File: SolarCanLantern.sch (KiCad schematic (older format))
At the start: 16 parts, among them Q1 2N7002, Q2 2N7002, Q3 2N7002, Q4 2N7002, U1 ATTINY13-20SSU

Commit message: add footprints
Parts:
- BT1, SC1: footprint (none) -> Socket_Strips:Socket_Strip_Straight_1x02_Pitch2.54mm
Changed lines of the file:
@@
 $EndComp
 $Comp
-L GND #PWR15
+L GND #PWR01
 U 1 1 5AC18C1B
 P 8200 3750
-F 0 "#PWR15" H 8200 3500 50  0001 C CNN
+F 0 "#PWR01" H 8200 3500 50  0001 C CNN
 F 1 "GND" H 8200 3600 50  0000 C CNN
 F 2 "" H 8200 3750 50  0001 C CNN
@@
 $EndComp
 $Comp
-L +BATT #PWR14
+L +BATT #PWR02
 U 1 1 5AC18C33
 P 8200 3100
-F 0 "#PWR14" H 8200 2950 50  0001 C CNN
+F 0 "#PWR02" H 8200 2950 50  0001 C CNN
 F 1 "+BATT" H 8200 3240 50  0000 C CNN
 F 2 "" H 8200 3100 50  0001 C CNN
@@
 	3250 2950 3250 3150
 $Comp
-L GND #PWR6
+L GND #PWR03
 U 1 1 5AC3EB93
 P 3250 3550
-F 0 "#PWR6" H 3250 3300 50  0001 C CNN
+F 0 "#PWR03" H 3250 3300 50  0001 C CNN
 F 1 "GND" H 3250 3400 50  0000 C CNN
 F 2 "" H 3250 3550 50  0001 C CNN
@@
 $EndComp
 $Comp
-L GND #PWR4
+L GND #PWR04
 U 1 1 5AC3EBB4
 P 2150 3550
-F 0 "#PWR4" H 2150 3300 50  0001 C CNN
+F 0 "#PWR04" H 2150 3300 50  0001 C CNN
 F 1 "GND" H 2150 3400 50  0000 C CNN
 F 2 "" H 2150 3550 50  0001 C CNN
@@
 $EndComp
 $Comp
-L +BATT #PWR3
+L +BATT #PWR05
 U 1 1 5AC3EBCE
 P 2150 2250
-F 0 "#PWR3" H 2150 2100 50  0001 C CNN
+F 0 "#PWR05" H 2150 2100 50  0001 C CNN
 F 1 "+BATT" H 2150 2390 50  0000 C CNN
 F 2 "" H 2150 2250 50  0001 C CNN
@@
 $EndComp
 $Comp
-L +BATT #PWR5
+L +BATT #PWR06
 U 1 1 5AC3EBE8
 P 3250 2250
-F 0 "#PWR5" H 3250 2100 50  0001 C CNN
+F 0 "#PWR06" H 3250 2100 50  0001 C CNN
 F 1 "+BATT" H 3250 2390 50  0000 C CNN
 F 2 "" H 3250 2250 50  0001 C CNN
@@
 	4450 2950 4450 3150
 $Comp
-L GND #PWR8
+L GND #PWR07
 U 1 1 5AC3EE60
 P 4450 3550
-F 0 "#PWR8" H 4450 3300 50  0001 C CNN
+F 0 "#PWR07" H 4450 3300 50  0001 C CNN
 F 1 "GND" H 4450 3400 50  0000 C CNN
 F 2 "" H 4450 3550 50  0001 C CNN
@@
 $EndComp
 $Comp
-L +BATT #PWR7
+L +BATT #PWR08
 U 1 1 5AC3EE66
 P 4450 2250
-F 0 "#PWR7" H 4450 2100 50  0001 C CNN
+F 0 "#PWR08" H 4450 2100 50  0001 C CNN
 F 1 "+BATT" H 4450 2390 50  0000 C CNN
 F 2 "" H 4450 2250 50  0001 C CNN
@@
 	5800 3550 5800 3750
 $Comp
-L GND #PWR9
+L GND #PWR09
 U 1 1 5AC3EF40
 P 5800 4050
-F 0 "#PWR9" H 5800 3800 50  0001 C CNN
+F 0 "#PWR09" H 5800 3800 50  0001 C CNN
 F 1 "GND" H 5800 3900 50  0000 C CNN
 F 2 "" H 5800 4050 50  0001 C CNN
@@
 Switch
 $Comp
-L +BATT #PWR1
+L +BATT #PWR010
 U 1 1 5AC3F242
 P 2100 4600
-F 0 "#PWR1" H 2100 4450 50  0001 C CNN
+F 0 "#PWR010" H 2100 4450 50  0001 C CNN
 F 1 "+BATT" H 2100 4740 50  0000 C CNN
 F 2 "" H 2100 4600 50  0001 C CNN
@@
 $EndComp
 $Comp
-L GND #PWR2
+L GND #PWR011
 U 1 1 5AC3F286
 P 2100 5400
-F 0 "#PWR2" H 2100 5150 50  0001 C CNN
+F 0 "#PWR011" H 2100 5150 50  0001 C CNN
 F 1 "GND" H 2100 5250 50  0000 C CNN
 F 2 "" H 2100 5400 50  0001 C CNN
@@
 F 0 "SC1" H 6800 1700 50  0000 L CNN
 F 1 "Solar_Cell" H 6800 1600 50  0000 L CNN
-F 2 "" V 6700 1660 50  0001 C CNN
+F 2 "Socket_Strips:Socket_Strip_Straight_1x02_Pitch2.54mm" V 6700 1660 50  0001 C CNN
 F 3 "" V 6700 1660 50  0001 C CNN
 	1    6700 1600
@@
 $EndComp
 $Comp
-L GND #PWR12
+L GND #PWR012
 U 1 1 5AC3F62A
 P 6400 2000
-F 0 "#PWR12" H 6400 1750 50  0001 C CNN
+F 0 "#PWR012" H 6400 1750 50  0001 C CNN
 F 1 "GND" H 6400 1850 50  0000 C CNN
 F 2 "" H 6400 2000 50  0001 C CNN
@@
 $EndComp
 $Comp
-L +BATT #PWR13
+L +BATT #PWR013
 U 1 1 5AC3F9A9
 P 7200 1250
-F 0 "#PWR13" H 7200 1100 50  0001 C CNN
+F 0 "#PWR013" H 7200 1100 50  0001 C CNN
 F 1 "+BATT" H 7200 1390 50  0000 C CNN
 F 2 "" H 7200 1250 50  0001 C CNN
@@
 F 0 "BT1" H 6000 5250 50  0000 L CNN
 F 1 "Battery_Cell" H 6000 5150 50  0000 L CNN
-F 2 "" V 5900 5210 50  0001 C CNN
+F 2 "Socket_Strips:Socket_Strip_Straight_1x02_Pitch2.54mm" V 5900 5210 50  0001 C CNN
 F 3 "" V 5900 5210 50  0001 C CNN
 	1    5900 5150
@@
 $EndComp
 $Comp
-L GND #PWR11
+L GND #PWR014
 U 1 1 5AC3FE84
 P 5900 5250
-F 0 "#PWR11" H 5900 5000 50  0001 C CNN
+F 0 "#PWR014" H 5900 5000 50  0001 C CNN
 F 1 "GND" H 5900 5100 50  0000 C CNN
 F 2 "" H 5900 5250 50  0001 C CNN
@@
 $EndComp
 $Comp
-L +BATT #PWR10
+L +BATT #PWR015
 U 1 1 5AC3FEBF
 P 5900 4950
-F 0 "#PWR10" H 5900 4800 50  0001 C CNN
+F 0 "#PWR015" H 5900 4800 50  0001 C CNN
 F 1 "+BATT" H 5900 5090 50  0000 C CNN
 F 2 "" H 5900 4950 50  0001 C CNN

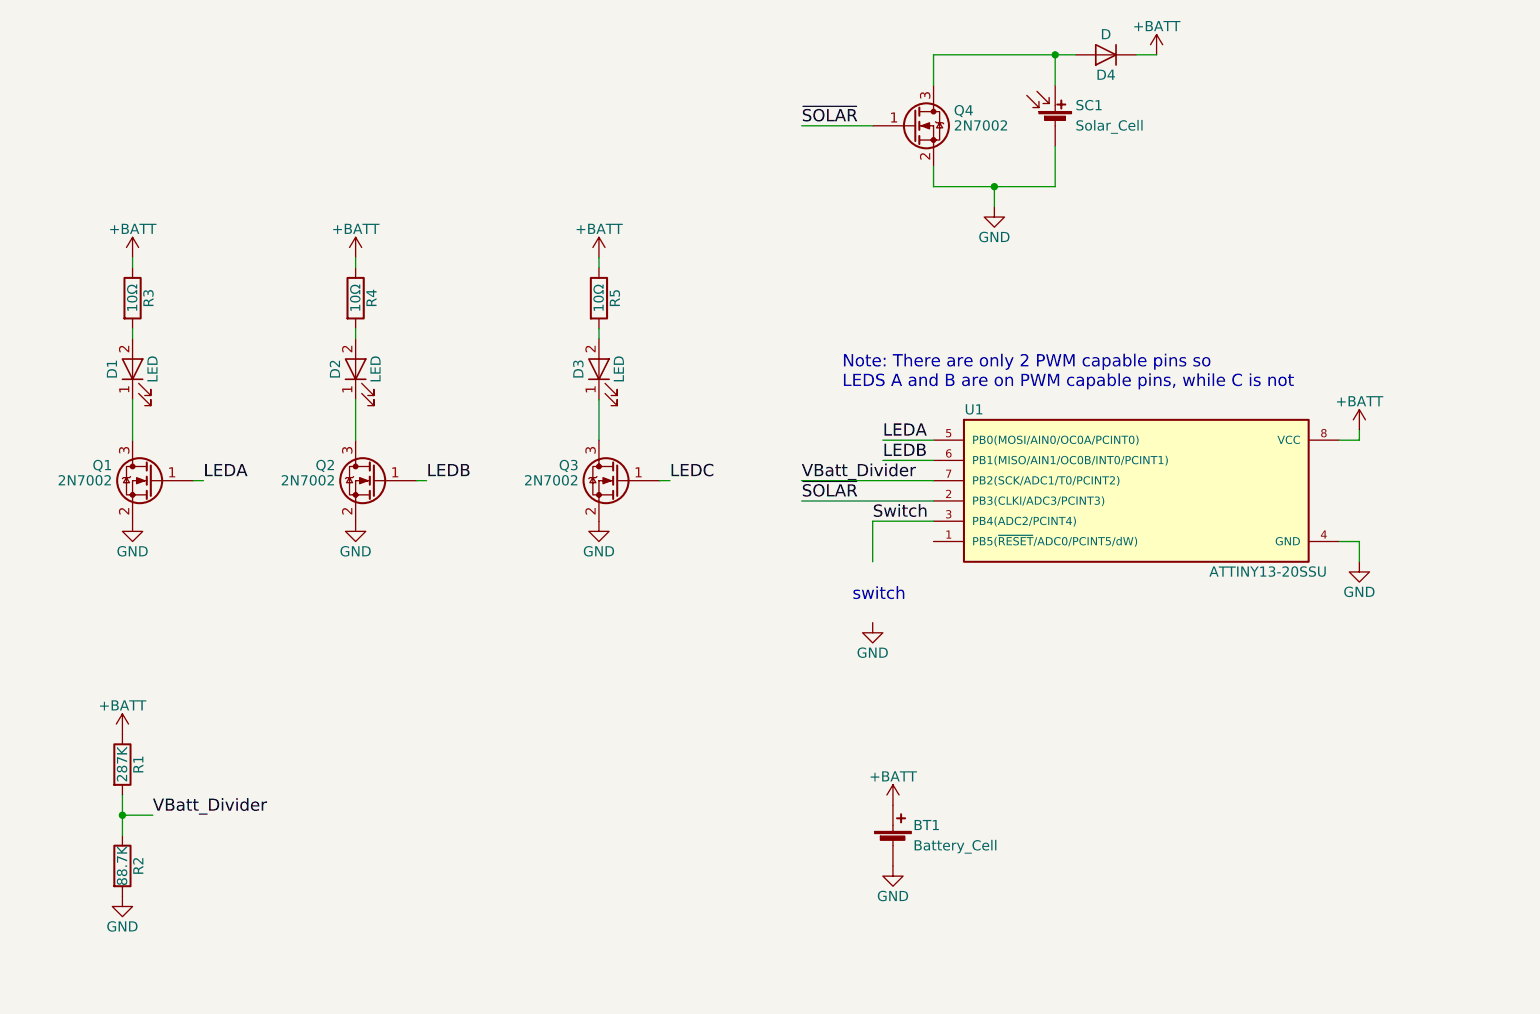
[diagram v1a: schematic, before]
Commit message: first rev pcb layout with no button
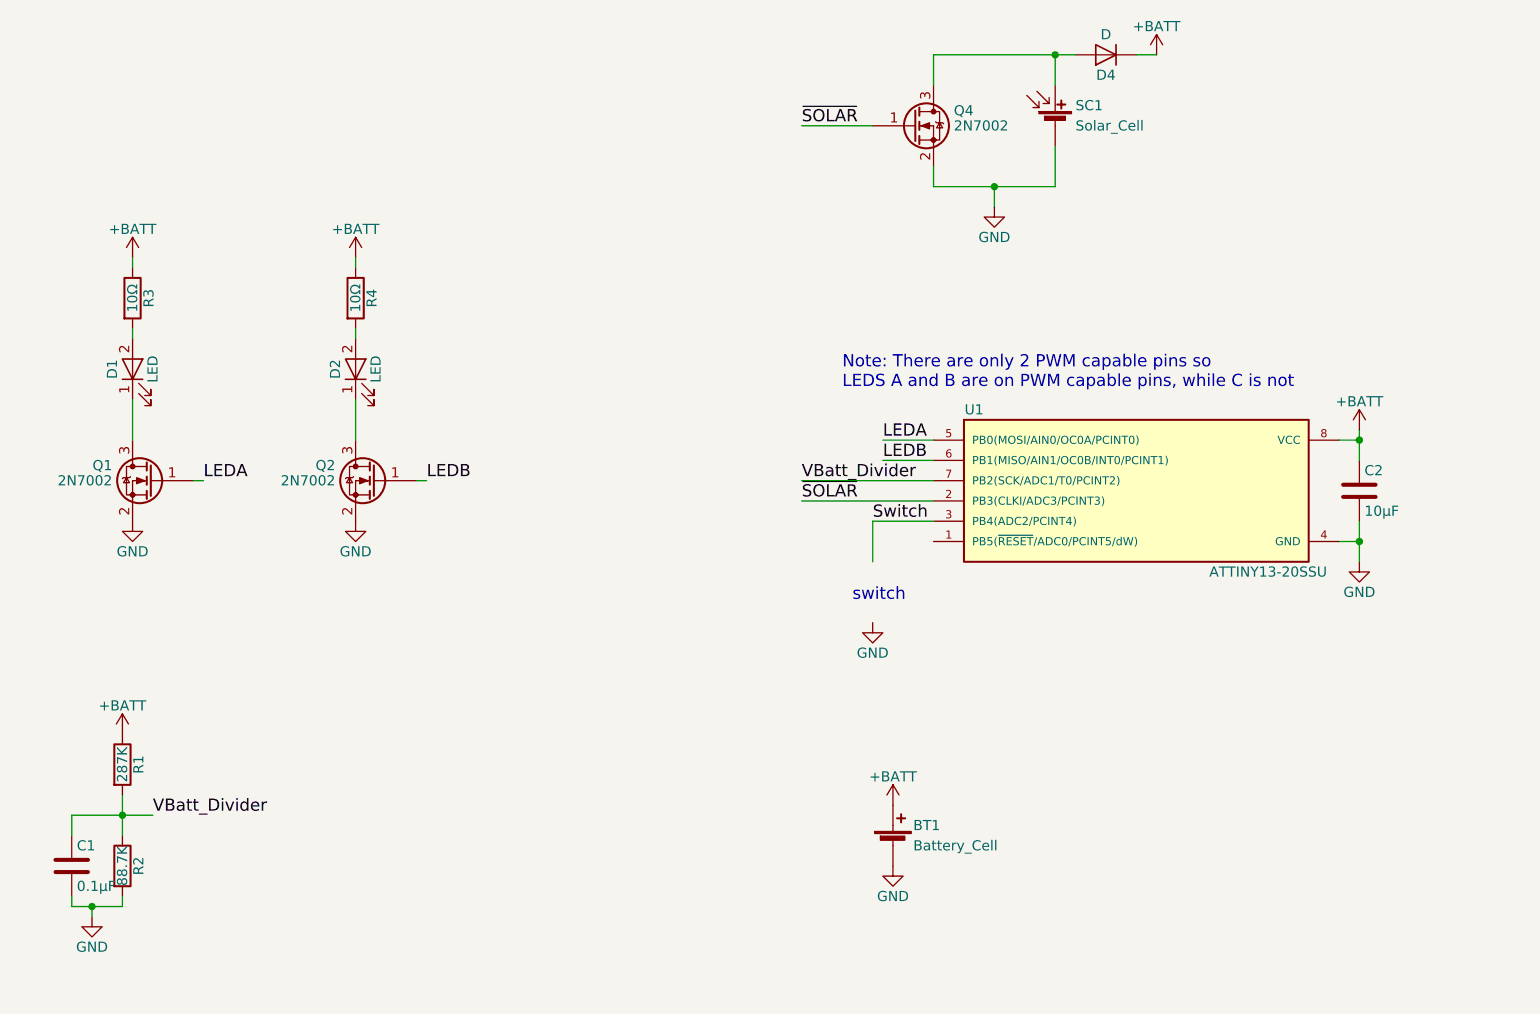
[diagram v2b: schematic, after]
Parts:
- removed D3: LED, LEDs:LED_0805_HandSoldering, symbol LED
- removed Q3: 2N7002, TO_SOT_Packages_SMD:SOT-23, symbol 2N7002
- removed R5: 10Ω, Resistors_SMD:R_0805_HandSoldering, symbol R
- added C1: 0.1µF, Capacitors_SMD:C_0805_HandSoldering, symbol C
- added C2: 10µF, Capacitors_SMD:C_0805_HandSoldering, symbol C
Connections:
- net +BATT: now also C2.1
- net GND: now also C1.2, C2.2
- net VBatt_Divider: now also C1.1
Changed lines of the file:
@@
 LIBS:contrib
 LIBS:valves
+LIBS:battery_management
+LIBS:74xgxx
+LIBS:Altera
+LIBS:analog_devices
+LIBS:dc-dc
+LIBS:stm32
 LIBS:SolarCanLantern-cache
 EELAYER 25 0
@@
 $EndComp
 Wire Wire Line
-	8200 3100 8200 3150
+	8200 3100 8200 3250
 Wire Wire Line
 	8200 3150 8100 3150
@@
 	8100 3650 8200 3650
 Wire Wire Line
-	8200 3650 8200 3750
+	8200 3550 8200 3750
 $Comp
 L LED D1
@@
 Wire Wire Line
 	3600 3350 3550 3350
-$Comp
-L LED D3
-U 1 1 5AC3EE53
-P 4450 2800
-F 0 "D3" H 4450 2900 50  0000 C CNN
-F 1 "LED" H 4450 2700 50  0000 C CNN
-F 2 "LEDs:LED_0805_HandSoldering" H 4450 2800 50  0001 C CNN
-F 3 "" H 4450 2800 50  0001 C CNN
-	1    4450 2800
-	0    -1   -1   0
-$EndComp
-$Comp
-L 2N7002 Q3
-U 1 1 5AC3EE59
-P 4550 3350
-F 0 "Q3" H 4750 3425 50  0000 L CNN
-F 1 "2N7002" H 4750 3350 50  0000 L CNN
-F 2 "TO_SOT_Packages_SMD:SOT-23" H 4750 3275 50  0001 L CIN
-F 3 "" H 4550 3350 50  0001 L CNN
-	1    4550 3350
-	-1   0    0    -1
-$EndComp
-Wire Wire Line
-	4450 2950 4450 3150
+Wire Wire Line
+	6100 3550 5800 3550
+Wire Wire Line
+	5800 3550 5800 3750
 $Comp
 L GND #PWR07
-U 1 1 5AC3EE60
-P 4450 3550
-F 0 "#PWR07" H 4450 3300 50  0001 C CNN
-F 1 "GND" H 4450 3400 50  0000 C CNN
-F 2 "" H 4450 3550 50  0001 C CNN
-F 3 "" H 4450 3550 50  0001 C CNN
-	1    4450 3550
-	1    0    0    -1
-$EndComp
-$Comp
-L +BATT #PWR08
-U 1 1 5AC3EE66
-P 4450 2250
-F 0 "#PWR08" H 4450 2100 50  0001 C CNN
-F 1 "+BATT" H 4450 2390 50  0000 C CNN
-F 2 "" H 4450 2250 50  0001 C CNN
-F 3 "" H 4450 2250 50  0001 C CNN
-	1    4450 2250
-	1    0    0    -1
-$EndComp
-$Comp
-L R R5
-U 1 1 5AC3EE6C
-P 4450 2450
-F 0 "R5" V 4530 2450 50  0000 C CNN
-F 1 "10Ω" V 4450 2450 50  0000 C CNN
-F 2 "Resistors_SMD:R_0805_HandSoldering" V 4380 2450 50  0001 C CNN
-F 3 "" H 4450 2450 50  0001 C CNN
-	1    4450 2450
-	1    0    0    -1
-$EndComp
-Wire Wire Line
-	4450 2600 4450 2650
-Wire Wire Line
-	4450 2300 4450 2250
-Text Label 4800 3350 0    60   ~ 0
-LEDC
-Wire Wire Line
-	4800 3350 4750 3350
-Wire Wire Line
-	6100 3550 5800 3550
-Wire Wire Line
-	5800 3550 5800 3750
-$Comp
-L GND #PWR09
 U 1 1 5AC3EF40
 P 5800 4050
-F 0 "#PWR09" H 5800 3800 50  0001 C CNN
+F 0 "#PWR07" H 5800 3800 50  0001 C CNN
 F 1 "GND" H 5800 3900 50  0000 C CNN
 F 2 "" H 5800 4050 50  0001 C CNN
@@
 Switch
 $Comp
-L +BATT #PWR010
+L +BATT #PWR08
 U 1 1 5AC3F242
 P 2100 4600
-F 0 "#PWR010" H 2100 4450 50  0001 C CNN
+F 0 "#PWR08" H 2100 4450 50  0001 C CNN
 F 1 "+BATT" H 2100 4740 50  0000 C CNN
 F 2 "" H 2100 4600 50  0001 C CNN
@@
 $EndComp
 $Comp
-L GND #PWR011
+L GND #PWR09
 U 1 1 5AC3F286
-P 2100 5400
-F 0 "#PWR011" H 2100 5150 50  0001 C CNN
-F 1 "GND" H 2100 5250 50  0000 C CNN
-F 2 "" H 2100 5400 50  0001 C CNN
-F 3 "" H 2100 5400 50  0001 C CNN
-	1    2100 5400
+P 1950 5500
+F 0 "#PWR09" H 1950 5250 50  0001 C CNN
+F 1 "GND" H 1950 5350 50  0000 C CNN
+F 2 "" H 1950 5500 50  0001 C CNN
+F 3 "" H 1950 5500 50  0001 C CNN
+	1    1950 5500
 	1    0    0    -1
 $EndComp
@@
 	2100 4900 2100 5100
 Wire Wire Line
-	2100 5000 2250 5000
+	1850 5000 2250 5000
 Connection ~ 2100 5000
 Text Label 2250 5000 0    60   ~ 0
@@
 $EndComp
 $Comp
-L GND #PWR012
+L GND #PWR010
 U 1 1 5AC3F62A
 P 6400 2000
-F 0 "#PWR012" H 6400 1750 50  0001 C CNN
+F 0 "#PWR010" H 6400 1750 50  0001 C CNN
 F 1 "GND" H 6400 1850 50  0000 C CNN
 F 2 "" H 6400 2000 50  0001 C CNN
@@
 $EndComp
 $Comp
-L +BATT #PWR013
+L +BATT #PWR011
 U 1 1 5AC3F9A9
 P 7200 1250
-F 0 "#PWR013" H 7200 1100 50  0001 C CNN
+F 0 "#PWR011" H 7200 1100 50  0001 C CNN
 F 1 "+BATT" H 7200 1390 50  0000 C CNN
 F 2 "" H 7200 1250 50  0001 C CNN
@@
 $EndComp
 $Comp
-L GND #PWR014
+L GND #PWR012
 U 1 1 5AC3FE84
 P 5900 5250
-F 0 "#PWR014" H 5900 5000 50  0001 C CNN
+F 0 "#PWR012" H 5900 5000 50  0001 C CNN
 F 1 "GND" H 5900 5100 50  0000 C CNN
 F 2 "" H 5900 5250 50  0001 C CNN
@@
 $EndComp
 $Comp
-L +BATT #PWR015
+L +BATT #PWR013
 U 1 1 5AC3FEBF
 P 5900 4950
-F 0 "#PWR015" H 5900 4800 50  0001 C CNN
+F 0 "#PWR013" H 5900 4800 50  0001 C CNN
 F 1 "+BATT" H 5900 5090 50  0000 C CNN
 F 2 "" H 5900 4950 50  0001 C CNN
@@
 Wire Wire Line
 	5450 3350 6100 3350
+$Comp
+L C C2
+U 1 1 5ADCFA52
+P 8200 3400
+F 0 "C2" H 8225 3500 50  0000 L CNN
+F 1 "10µF" H 8225 3300 50  0000 L CNN
+F 2 "Capacitors_SMD:C_0805_HandSoldering" H 8238 3250 50  0001 C CNN
+F 3 "" H 8200 3400 50  0001 C CNN
+	1    8200 3400
+	1    0    0    -1
+$EndComp
+Connection ~ 8200 3150
+Connection ~ 8200 3650
+$Comp
+L C C1
+U 1 1 5ADCFBF2
+P 1850 5250
+F 0 "C1" H 1875 5350 50  0000 L CNN
+F 1 "0.1µF" H 1875 5150 50  0000 L CNN
+F 2 "Capacitors_SMD:C_0805_HandSoldering" H 1888 5100 50  0001 C CNN
+F 3 "" H 1850 5250 50  0001 C CNN
+	1    1850 5250
+	1    0    0    -1
+$EndComp
+Wire Wire Line
+	1850 5100 1850 5000
+Wire Wire Line
+	2100 5400 2100 5450
+Wire Wire Line
+	2100 5450 1850 5450
+Wire Wire Line
+	1850 5450 1850 5400
+Wire Wire Line
+	1950 5450 1950 5500
+Connection ~ 1950 5450
 $EndSCHEMATC

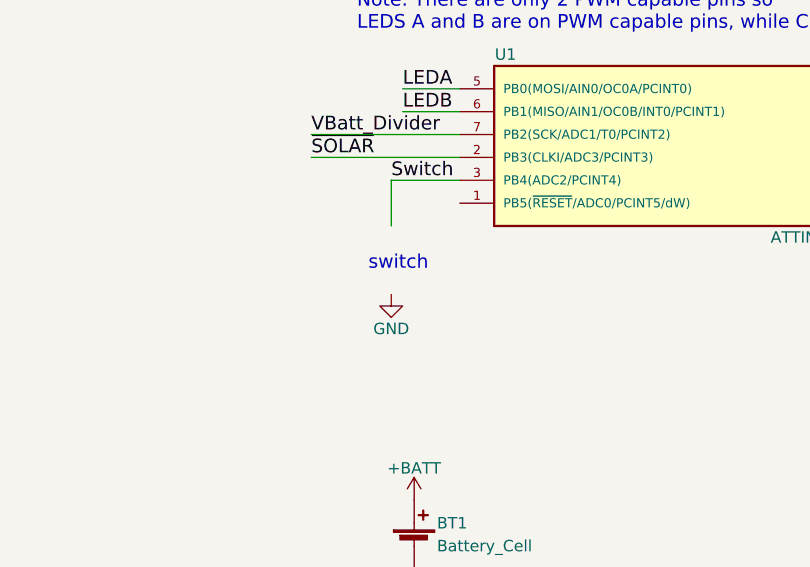
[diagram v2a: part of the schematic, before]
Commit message: Added switch and completed first PCB layout
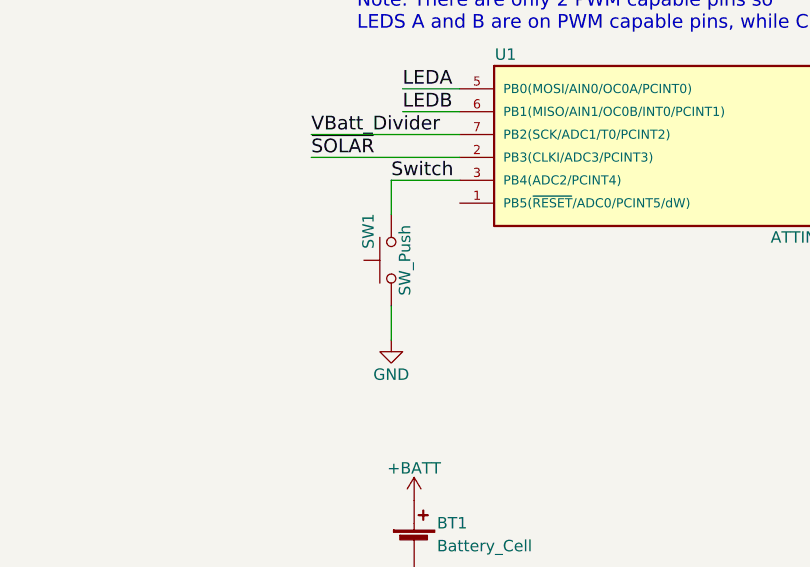
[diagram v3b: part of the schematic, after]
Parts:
- added SW1: SW_Push, Buttons_Switches_THT:SW_Tactile_SKHH_Angled, symbol SW_Push
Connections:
- net GND: now also SW1.1
- net Switch: now also SW1.2
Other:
- note removed: "switch\n"
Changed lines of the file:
@@
 LIBS:dc-dc
 LIBS:stm32
+LIBS:switches
 LIBS:SolarCanLantern-cache
 EELAYER 25 0
@@
 Wire Wire Line
 	6100 3550 5800 3550
-Wire Wire Line
-	5800 3550 5800 3750
 $Comp
 L GND #PWR07
 U 1 1 5AC3EF40
-P 5800 4050
-F 0 "#PWR07" H 5800 3800 50  0001 C CNN
-F 1 "GND" H 5800 3900 50  0000 C CNN
-F 2 "" H 5800 4050 50  0001 C CNN
-F 3 "" H 5800 4050 50  0001 C CNN
-	1    5800 4050
-	1    0    0    -1
-$EndComp
-Text Notes 5700 3950 0    60   ~ 0
-switch\n
+P 5800 4250
+F 0 "#PWR07" H 5800 4000 50  0001 C CNN
+F 1 "GND" H 5800 4100 50  0000 C CNN
+F 2 "" H 5800 4250 50  0001 C CNN
+F 3 "" H 5800 4250 50  0001 C CNN
+	1    5800 4250
+	1    0    0    -1
+$EndComp
 Text Label 5850 3150 0    60   ~ 0
 LEDA
@@
 	1950 5450 1950 5500
 Connection ~ 1950 5450
+$Comp
+L SW_Push SW1
+U 1 1 5AEB74F4
+P 5800 3900
+F 0 "SW1" H 5850 4000 50  0000 L CNN
+F 1 "SW_Push" H 5800 3840 50  0000 C CNN
+F 2 "Buttons_Switches_THT:SW_Tactile_SKHH_Angled" H 5800 4100 50  0001 C CNN
+F 3 "" H 5800 4100 50  0001 C CNN
+	1    5800 3900
+	0    -1   -1   0
+$EndComp
+Wire Wire Line
+	5800 4250 5800 4100
+Wire Wire Line
+	5800 3550 5800 3700
 $EndSCHEMATC

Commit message: got latest version from tejus and modified
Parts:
- removed D4: D, Diodes_SMD:D_0805, symbol D
- removed Q4: 2N7002, TO_SOT_Packages_SMD:SOT-23, symbol 2N7002
- added U2: MAX40200, TO_SOT_Packages_SMD:TSOT-23-5_HandSoldering, symbol SolarCanLantern:MAX40200
- BT1: symbol Battery_Cell -> Device:Battery_Cell
- C1, C2: symbol C -> Device:C
- D1, D2: symbol LED -> Device:LED
- Q1, Q2: symbol 2N7002 -> SolarCanLantern-rescue:2N7002
- R1, R2, R3, R4: symbol R -> Device:R
- SC1: symbol Solar_Cell -> Device:Solar_Cell
- SW1: symbol SW_Push -> SolarCanLantern-rescue:SW_Push
- U1: symbol ATTINY13-20SSU -> SolarCanLantern-rescue:ATTINY13-20SSU
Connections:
- net labels added: SolarIn
- wire segments 35 -> 36
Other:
- moved on the sheet: BT1, C1, C2, D1, D2, Q1, Q2, R1, R2, R3, R4, SC1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

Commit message: slightly reorganize board
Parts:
- BT1, SC1: footprint Socket_Strips:Socket_Strip_Straight_1x02_Pitch2.54mm -> Socket_Strips:Socket_Strip_Straight_1x02_Pitch2.00mm
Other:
- moved on the sheet: BT1, C1, D1, D2, Q1, Q2, R1, R2, R3, R4, SC1
